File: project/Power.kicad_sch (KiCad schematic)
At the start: 20 parts, among them IC101 nPM1300-QEXX, X101 BATTERY

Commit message: Change layer for PCB tables to User1
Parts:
- C101, C110: Order Number 581-0603YC105JAT2A -> (none); Order. No. (none) -> 581-0603YC105JAT2A
- C102: Order Number 581-06035C104KAT2A -> (none); Order. No. (none) -> 581-06035C104KAT2A
- C103: Order Number 581-06036D225KAT2A -> (none); Order. No. (none) -> 581-06036D225KAT2A
- C104, C105, C106, C107, C108, C109: Order Number 346-CM105X5R106M25AT -> (none); Order. No. (none) -> 346-CM105X5R106M25AT
- IC101: Order Number 949-NPM1300-QEAA-R7 -> (none); Order. No. (none) -> 949-NPM1300-QEAA-R7
- L101, L102: Order Number 187-CIGT201610EH2R2M -> (none); Order. No. (none) -> 187-CIGT201610EH2R2MNE
- R101: Order Number 603-RC0603FR-0747KL -> (none); Order. No. (none) -> 603-RC0603FR-0747KL
- R102: Order Number 603-RC0603FR-07150KL -> (none); Order. No. (none) -> 603-RC0603FR-07150KL
- R103: Order Number 652-CR0603-J/-000ELF -> (none); Order. No. (none) -> 652-CR0603-J/-000ELF
- X101: Order Number 538-78171-0002 -> (none); Order. No. (none) -> 538-78171-0002
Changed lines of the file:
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@@
 			)
 		)
-		(property "Datasheet" "~"
+		(property "Datasheet" "https://www.mouser.de/datasheet/2/40/KGM_X7R-3223212.pdf"
 			(at 218.44 91.44 0)
 			(effects
@@
 			)
 		)
-		(property "Order Number" "581-0603YC105JAT2A"
+		(property "CONFIG" ""
 			(at 218.44 91.44 0)
 			(effects
@@
 			)
 		)
-		(property "CONFIG" ""
+		(property "Order. No." "581-0603YC105JAT2A"
 			(at 218.44 91.44 0)
 			(effects
@@
 			)
 		)
-		(property "Datasheet" "~"
+		(property "Datasheet" "https://www.mouser.de/datasheet/2/585/sems_s_a0006918008_1-2288745.pdf"
 			(at 173.99 106.68 0)
 			(effects
@@
 			)
 		)
-		(property "Order Number" "187-CIGT201610EH2R2M"
+		(property "CONFIG" ""
 			(at 173.99 106.68 0)
 			(effects
@@
 			)
 		)
-		(property "CONFIG" ""
+		(property "Order. No." "187-CIGT201610EH2R2MNE"
 			(at 173.99 106.68 0)
 			(effects
@@
 			)
 		)
-		(property "Datasheet" "~"
+		(property "Datasheet" "https://www.mouser.de/datasheet/2/40/KGM_X7R-3223212.pdf"
 			(at 113.03 44.45 0)
 			(effects
@@
 			)
 		)
-		(property "Order Number" "581-0603YC105JAT2A"
+		(property "CONFIG" ""
 			(at 113.03 44.45 0)
 			(effects
@@
 			)
 		)
-		(property "CONFIG" ""
+		(property "Order. No." "581-0603YC105JAT2A"
 			(at 113.03 44.45 0)
 			(effects
@@
 			)
 		)
-		(property "Datasheet" "~"
+		(property "Datasheet" "https://www.mouser.de/datasheet/2/40/CM_Series_e-2835982.pdf"
 			(at 184.15 109.22 0)
 			(effects
@@
 			)
 		)
-		(property "Order Number" "346-CM105X5R106M25AT"
+		(property "CONFIG" ""
 			(at 184.15 109.22 0)
 			(effects
@@
 			)
 		)
-		(property "CONFIG" ""
+		(property "Order. No." "346-CM105X5R106M25AT"
 			(at 184.15 109.22 0)
 			(effects
@@
 			)
 		)
-		(property "Order Number" "603-RC0603FR-07150KL"
+		(property "CONFIG" ""
 			(at 82.55 134.62 0)
 			(effects
@@
 			)
 		)
-		(property "CONFIG" ""
+		(property "Order. No." "603-RC0603FR-07150KL"
 			(at 82.55 134.62 0)
 			(effects
@@
 			)
 		)
-		(property "Order Number" ""
-			(at 200.66 125.73 0)
-			(effects
-				(font
-					(size 1.27 1.27)
-				)
-				(hide yes)
-			)
-		)
 		(property "CONFIG" ""
 			(at 200.66 125.73 0)
@@
 			)
 		)
-		(property "Datasheet" "~"
+		(property "Datasheet" "https://www.mouser.de/datasheet/2/40/CM_Series_e-2835982.pdf"
 			(at 193.04 91.44 0)
 			(effects
@@
 			)
 		)
-		(property "Order Number" "346-CM105X5R106M25AT"
+		(property "CONFIG" ""
 			(at 193.04 91.44 0)
 			(effects
@@
 			)
 		)
-		(property "CONFIG" ""
+		(property "Order. No." "346-CM105X5R106M25AT"
 			(at 193.04 91.44 0)
 			(effects
@@
 			)
 		)
-		(property "Order Number" "603-RC0603FR-0747KL"
+		(property "CONFIG" ""
 			(at 80.01 134.62 0)
 			(effects
@@
 			)
 		)
-		(property "CONFIG" ""
+		(property "Order. No." "603-RC0603FR-0747KL"
 			(at 80.01 134.62 0)
 			(effects
@@
 			)
 		)
-		(property "Order Number" "949-NPM1300-QEAA-R7"
+		(property "CONFIG" ""
 			(at 132.08 107.95 0)
 			(effects
@@
 			)
 		)
-		(property "CONFIG" ""
+		(property "Order. No." "949-NPM1300-QEAA-R7"
 			(at 132.08 107.95 0)
 			(effects
@@
 			)
 		)
-		(property "Datasheet" "~"
+		(property "Datasheet" "https://www.mouser.de/datasheet/2/40/CM_Series_e-2835982.pdf"
 			(at 191.77 63.5 0)
 			(effects
@@
 			)
 		)
-		(property "Order Number" "346-CM105X5R106M25AT"
+		(property "CONFIG" ""
 			(at 191.77 63.5 0)
 			(effects
@@
 			)
 		)
-		(property "CONFIG" ""
+		(property "Order. No." "346-CM105X5R106M25AT"
 			(at 191.77 63.5 0)
 			(effects
@@
 			)
 		)
-		(property "Datasheet" "~"
+		(property "Datasheet" "https://www.mouser.de/datasheet/2/585/sems_s_a0006918008_1-2288745.pdf"
 			(at 182.88 88.9 0)
 			(effects
@@
 			)
 		)
-		(property "Order Number" "187-CIGT201610EH2R2M"
+		(property "CONFIG" ""
 			(at 182.88 88.9 0)
 			(effects
@@
 			)
 		)
-		(property "CONFIG" ""
+		(property "Order. No." "187-CIGT201610EH2R2MNE"
 			(at 182.88 88.9 0)
 			(effects
@@
 			)
 		)
-		(property "Order Number" "538-78171-0002"
+		(property "CONFIG" ""
 			(at 158.75 40.64 0)
 			(effects
@@
 			)
 		)
-		(property "CONFIG" ""
+		(property "Order. No." "538-78171-0002"
 			(at 158.75 40.64 0)
 			(effects
@@
 			)
 		)
-		(property "Datasheet" "~"
+		(property "Datasheet" "https://www.mouser.de/datasheet/2/54/cr-1858361.pdf"
 			(at 135.89 63.5 0)
 			(effects
@@
 			)
 		)
-		(property "Order Number" "652-CR0603-J/-000ELF"
+		(property "CONFIG" ""
 			(at 135.89 63.5 0)
 			(effects
@@
 			)
 		)
-		(property "CONFIG" ""
+		(property "Order. No." "652-CR0603-J/-000ELF"
 			(at 135.89 63.5 0)
 			(effects
@@
 			)
 		)
-		(property "Datasheet" "~"
+		(property "Datasheet" "https://www.mouser.de/datasheet/2/40/CM_Series_e-2835982.pdf"
 			(at 181.61 63.5 0)
 			(effects
@@
 			)
 		)
-		(property "Order Number" "346-CM105X5R106M25AT"
+		(property "CONFIG" ""
 			(at 181.61 63.5 0)
 			(effects
@@
 			)
 		)
-		(property "CONFIG" ""
+		(property "Order. No." "346-CM105X5R106M25AT"
 			(at 181.61 63.5 0)
 			(effects
@@
 			)
 		)
-		(property "Datasheet" "~"
+		(property "Datasheet" "https://www.mouser.de/datasheet/2/40/cx5r_KGM-3223198.pdf"
 			(at 140.97 44.45 0)
 			(effects
@@
 			)
 		)
-		(property "Order Number" "581-06036D225KAT2A"
+		(property "CONFIG" ""
 			(at 140.97 44.45 0)
 			(effects
@@
 			)
 		)
-		(property "CONFIG" ""
+		(property "Order. No." "581-06036D225KAT2A"
 			(at 140.97 44.45 0)
 			(effects
@@
 			)
 		)
-		(property "Datasheet" "~"
+		(property "Datasheet" "https://www.mouser.de/datasheet/2/40/CM_Series_e-2835982.pdf"
 			(at 200.66 132.08 0)
 			(effects
@@
 			)
 		)
-		(property "Order Number" "346-CM105X5R106M25AT"
+		(property "CONFIG" ""
 			(at 200.66 132.08 0)
 			(effects
@@
 			)
 		)
-		(property "CONFIG" ""
+		(property "Order. No." "346-CM105X5R106M25AT"
 			(at 200.66 132.08 0)
 			(effects
@@
 			)
 		)
-		(property "Order Number" ""
-			(at 200.66 104.14 0)
-			(effects
-				(font
-					(size 1.27 1.27)
-				)
-				(hide yes)
-			)
-		)
 		(property "CONFIG" ""
 			(at 200.66 104.14 0)
@@
 			)
 		)
-		(property "Datasheet" "~"
+		(property "Datasheet" "https://www.mouser.de/datasheet/2/40/KGM_X7R-3223212.pdf"
 			(at 128.27 44.45 0)
 			(effects
@@
 			)
 		)
-		(property "Order Number" "581-06035C104KAT2A"
+		(property "CONFIG" ""
 			(at 128.27 44.45 0)
 			(effects
@@
 			)
 		)
-		(property "CONFIG" ""
+		(property "Order. No." "581-06035C104KAT2A"
 			(at 128.27 44.45 0)
 			(effects
@@
 			)
 		)
-		(property "Datasheet" "~"
+		(property "Datasheet" "https://www.mouser.de/datasheet/2/40/CM_Series_e-2835982.pdf"
 			(at 201.93 63.5 0)
 			(effects
@@
 			)
 		)
-		(property "Order Number" "346-CM105X5R106M25AT"
+		(property "CONFIG" ""
 			(at 201.93 63.5 0)
 			(effects
@@
 			)
 		)
-		(property "CONFIG" ""
+		(property "Order. No." "346-CM105X5R106M25AT"
 			(at 201.93 63.5 0)
 			(effects
@@
 			(at 200.66 86.36 0)
 			(effects
-				(font
-					(size 1.27 1.27)
-				)
-				(hide yes)
-			)
-		)
-		(property "Order Number" ""
-			(at 200.66 86.36 0)
-			(effects

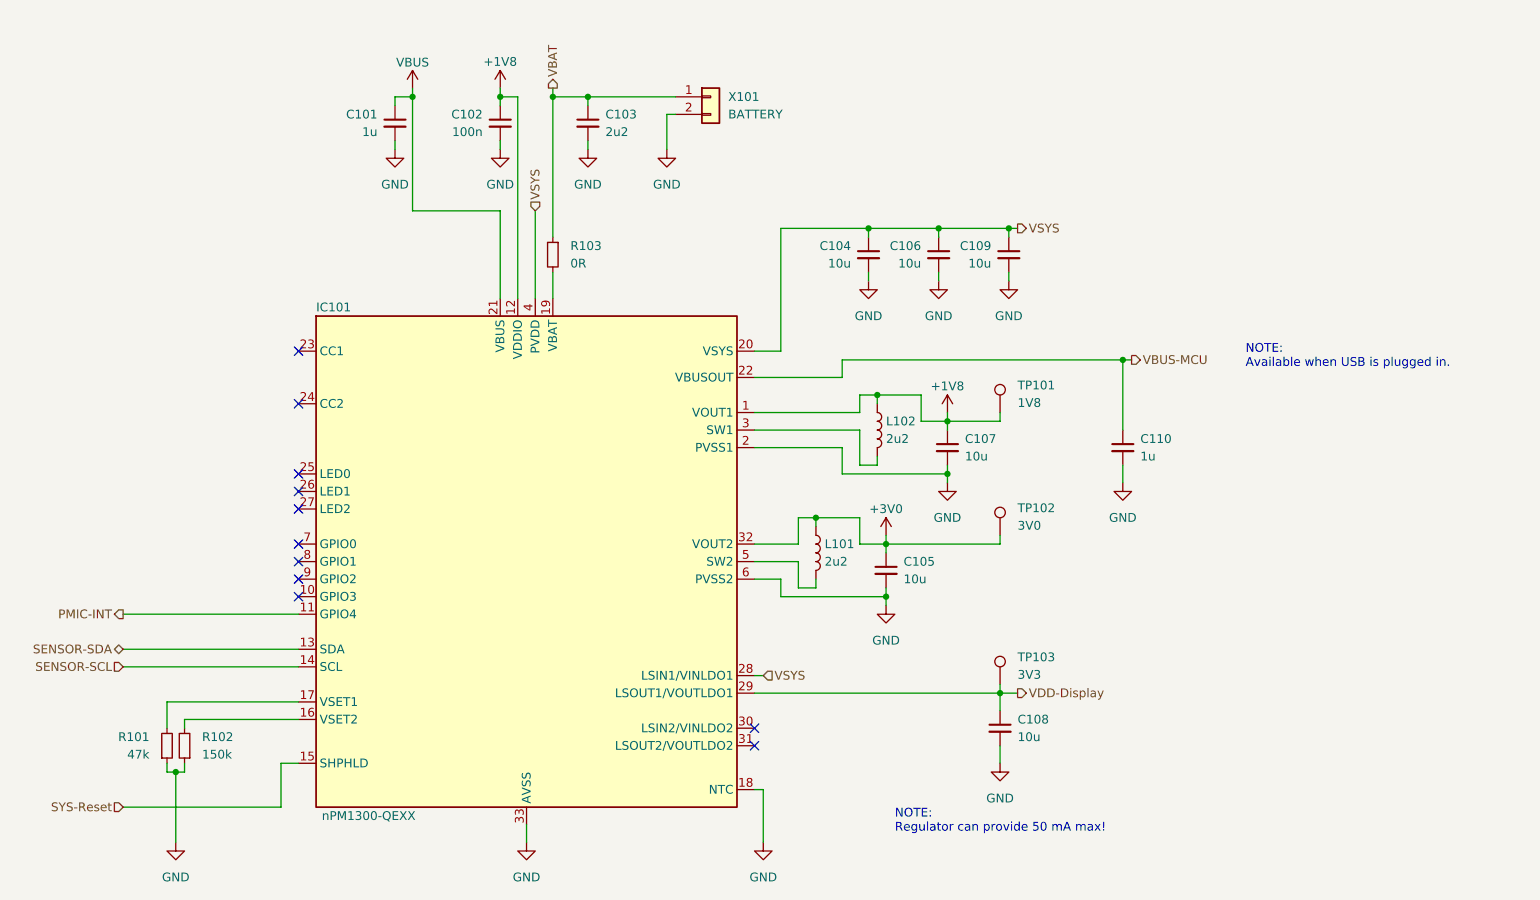
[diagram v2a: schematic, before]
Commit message: Rename signals and update symbols and footprints
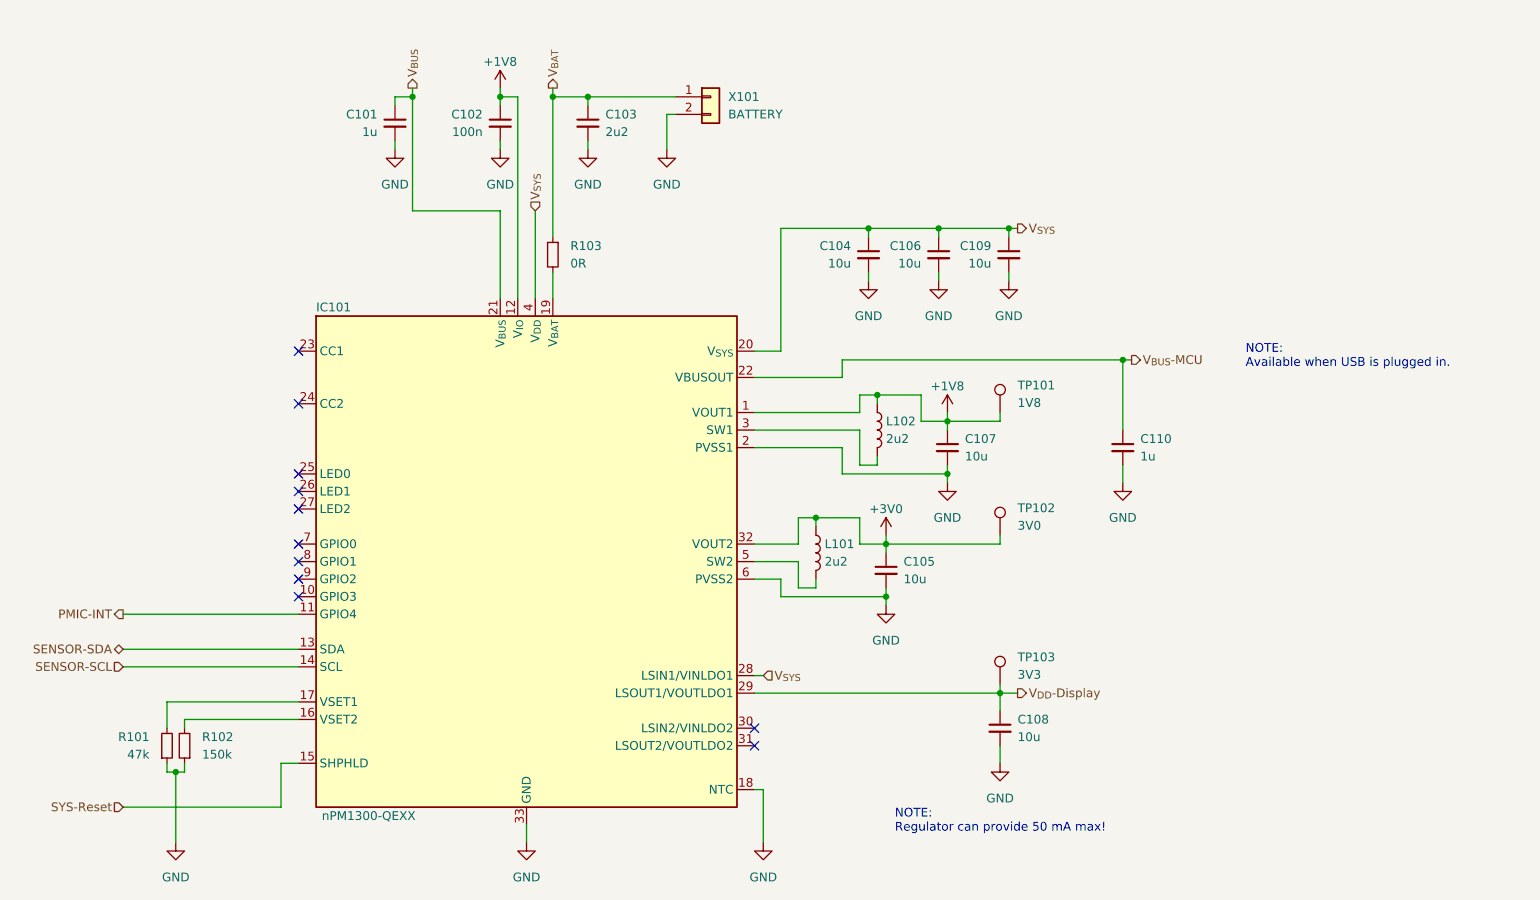
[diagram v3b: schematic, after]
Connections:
- net VBAT renamed V_{BAT}
- net VBUS renamed V_{BUS}
- net VBUS-MCU renamed V_{BUS}-MCU
- net VDD-Display renamed V_{DD}-Display
- net VSYS renamed V_{SYS}
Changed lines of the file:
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@@
 		)
 	)
-	(hierarchical_label "VSYS"
+	(hierarchical_label "V_{SYS}"
 		(shape output)
 		(at 203.2 59.69 0)
@@
 		)
 	)
-	(hierarchical_label "VBAT"
+	(hierarchical_label "V_{BAT}"
 		(shape output)
 		(at 135.89 39.37 90)
@@
 		)
 	)
-	(hierarchical_label "VBUS-MCU"
+	(hierarchical_label "V_{BUS}-MCU"
 		(shape output)
 		(at 219.71 78.74 0)
@@
 		)
 	)
-	(hierarchical_label "VSYS"
+	(hierarchical_label "V_{SYS}"
 		(shape input)
 		(at 166.37 124.46 0)
@@
 		)
 	)
-	(hierarchical_label "VDD-Display"
+	(hierarchical_label "V_{BUS}"
+		(shape output)
+		(at 115.57 39.37 90)
+		(fields_autoplaced yes)
+		(effects
+			(font
+				(size 1.27 1.27)
+			)
+			(justify left)
+		)
+	)
+	(hierarchical_label "V_{DD}-Display"
 		(shape output)
 		(at 203.2 127 0)
@@
 		)
 	)
-	(hierarchical_label "VSYS"
+	(hierarchical_label "V_{SYS}"
 		(shape input)
 		(at 133.35 57.15 90)
@@
 			)
 		)
-		(property "Description" ""
+		(property "Description" "Power symbol creates a global label with name \"GND\" , ground"
 			(at 184.15 114.3 0)
 			(effects
@@
 			)
 		)
-		(property "Description" ""
+		(property "Description" "Power symbol creates a global label with name \"+1V8\""
+			(at 128.27 39.37 0)
+			(effects
+				(font
+					(size 1.27 1.27)
+				)
+				(hide yes)
+			)
+		)
+		(property "Mfr." ""
+			(at 128.27 39.37 0)
+			(effects
+				(font
+					(size 1.27 1.27)
+				)
+				(hide yes)
+			)
+		)
+		(property "Mfr. No." ""
+			(at 128.27 39.37 0)
+			(effects
+				(font
+					(size 1.27 1.27)
+				)
+				(hide yes)
+			)
+		)
+		(property "Distributor" ""
+			(at 128.27 39.37 0)
+			(effects
+				(font
+					(size 1.27 1.27)
+				)
+				(hide yes)
+			)
+		)
+		(property "Order No." ""
+			(at 128.27 39.37 0)
+			(effects
+				(font
+					(size 1.27 1.27)
+				)
+				(hide yes)
+			)
+		)
+		(property "CONFIG" ""
 			(at 128.27 39.37 0)
 			(effects
@@
 			)
 		)
-		(property "Description" ""
+		(property "Description" "Power symbol creates a global label with name \"GND\" , ground"
 			(at 191.77 67.31 0)
 			(effects
@@
 			)
 		)
-		(property "Datasheet" "https://docs.nordicsemi.com/category/npm1300-category"
+		(property "Datasheet" "https://infocenter.nordicsemi.com/index.jsp?topic=%2Fstruct_pmic%2Fstruct%2Fnpm1300.html"
 			(at 132.08 110.49 0)
 			(effects
@@
 			)
 		)
+		(property "Order No." ""
+			(at 132.08 107.95 0)
+			(effects
+				(font
+					(size 1.27 1.27)
+				)
+				(hide yes)
+			)
+		)
 		(pin "1"
 		)
@@
 			)
 		)
-		(property "Description" ""
+		(property "Description" "Power symbol creates a global label with name \"+3V0\""
+			(at 184.15 104.14 0)
+			(effects
+				(font
+					(size 1.27 1.27)
+				)
+				(hide yes)
+			)
+		)
+		(property "Mfr." ""
+			(at 184.15 104.14 0)
+			(effects
+				(font
+					(size 1.27 1.27)
+				)
+				(hide yes)
+			)
+		)
+		(property "Mfr. No." ""
+			(at 184.15 104.14 0)
+			(effects
+				(font
+					(size 1.27 1.27)
+				)
+				(hide yes)
+			)
+		)
+		(property "Distributor" ""
+			(at 184.15 104.14 0)
+			(effects
+				(font
+					(size 1.27 1.27)
+				)
+				(hide yes)
+			)
+		)
+		(property "Order No." ""
+			(at 184.15 104.14 0)
+			(effects
+				(font
+					(size 1.27 1.27)
+				)
+				(hide yes)
+			)
+		)
+		(property "CONFIG" ""
 			(at 184.15 104.14 0)
 			(effects
@@
 			)
 		)
-		(property "Description" ""
+		(property "Description" "Power symbol creates a global label with name \"GND\" , ground"
 			(at 152.4 48.26 0)
 			(effects
@@
 			)
 		)
-		(property "Description" ""
+		(property "Description" "Power symbol creates a global label with name \"GND\" , ground"
 			(at 201.93 67.31 0)
 			(effects
@@
 			)
 		)
-		(property "Description" ""
+		(property "Description" "Power symbol creates a global label with name \"GND\" , ground"
 			(at 132.08 148.59 0)
 			(effects
@@
 			)
 		)
-		(property "Description" ""
+		(property "Description" "Power symbol creates a global label with name \"GND\" , ground"
 			(at 113.03 48.26 0)
 			(effects
@@
 			)
 		)
-		(property "Description" ""
+		(property "Description" "Power symbol creates a global label with name \"GND\" , ground"
 			(at 181.61 67.31 0)
 			(effects
@@
 			)
 		)
+		(property "Order No." ""
+			(at 181.61 67.31 0)
+			(effects
+				(font
+					(size 1.27 1.27)
+				)
+				(hide yes)
+			)
+		)
+		(property "CONFIG" ""
+			(at 181.61 67.31 0)
+			(effects
+				(font
+					(size 1.27 1.27)
+				)
+				(hide yes)
+			)
+		)
 		(pin "1"
 		)
@@
 			)
 		)
-		(property "Description" ""
+		(property "Description" "Power symbol creates a global label with name \"GND\" , ground"
 			(at 200.66 137.16 0)
 			(effects
@@
 			)
 		)
-		(property "Description" ""
+		(property "Description" "Power symbol creates a global label with name \"+1V8\""
 			(at 193.04 86.36 0)
 			(effects
@@
 			)
 		)
-		(property "Description" ""
+		(property "Description" "Power symbol creates a global label with name \"GND\" , ground"
 			(at 218.44 96.52 0)
 			(effects
@@
 	)
 	(symbol
-		(lib_id "power:VBUS")
-		(at 115.57 39.37 0)
-		(mirror y)
-		(unit 1)
-		(exclude_from_sim no)
-		(in_bom yes)
-		(on_board yes)
-		(dnp no)
-		(property "Reference" "#PWR0103"
-			(at 115.57 43.18 0)
-			(effects
-				(font
-					(size 1.27 1.27)
-				)
-				(hide yes)
-			)
-		)
-		(property "Value" "VBUS"
-			(at 115.57 35.6616 0)
-			(effects
-				(font
-					(size 1.27 1.27)
-				)
-			)
-		)
-		(property "Footprint" ""
-			(at 115.57 39.37 0)
-			(effects
-				(font
-					(size 1.27 1.27)
-				)
-				(hide yes)
-			)
-		)
-		(property "Datasheet" ""
-			(at 115.57 39.37 0)
-			(effects
-				(font
-					(size 1.27 1.27)
-				)
-				(hide yes)
-			)
-		)
-		(property "Description" ""
-			(at 115.57 39.37 0)
-			(effects
-				(font
-					(size 1.27 1.27)
-				)
-				(hide yes)
-			)
-		)
-		(property "Mfr." ""
-			(at 115.57 39.37 0)
-			(effects
-				(font
-					(size 1.27 1.27)
-				)
-				(hide yes)
-			)
-		)
-		(property "Mfr. No." ""
-			(at 115.57 39.37 0)
-			(effects
-				(font
-					(size 1.27 1.27)
-				)
-				(hide yes)
-			)
-		)
-		(property "Distributor" ""
-			(at 115.57 39.37 0)
-			(effects
-				(font
-					(size 1.27 1.27)
-				)
-				(hide yes)
-			)
-		)
-		(property "Order Number" ""
-			(at 115.57 39.37 0)
-			(effects
-				(font
-					(size 1.27 1.27)
-				)
-				(hide yes)
-			)
-		)
-		(pin "1"
-		)
-		(instances
-			(project "ZSWatch"
-				(path "/d5742f03-3b1a-42e5-a384-018bd4b919aa/cee9a3a2-28cd-4e6c-b23d-337f115f39e8"
-					(reference "#PWR0103")
-					(unit 1)
-				)
-			)
-		)
-	)
-	(symbol
 		(lib_id "Device:C_Small")
 		(at 128.27 44.45 0)
@@
 			)
 		)
-		(property "Description" ""
+		(property "Description" "Power symbol creates a global label with name \"GND\" , ground"
 			(at 166.37 148.59 0)
 			(effects
@@
 			)
 		)
-		(property "Description" ""
+		(property "Description" "Power symbol creates a global label with name \"GND\" , ground"
 			(at 140.97 48.26 0)
 			(effects
@@
 			)
 		)
-		(property "Description" ""
+		(property "Description" "Power symbol creates a global label with name \"GND\" , ground"
 			(at 193.04 96.52 0)
 			(effects
@@
 			)
 		)
-		(property "Description" ""
+		(property "Description" "Power symbol creates a global label with name \"GND\" , ground"
 			(at 128.27 48.26 0)
 			(effects
@@
 			)
 		)
-		(property "Description" ""
+		(property "Description" "Power symbol creates a global label with name \"GND\" , ground"
 			(at 81.28 148.59 0)
 			(effects

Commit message: - Switch to a local KiCad library
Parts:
- IC101: footprint Package_DFN_QFN:QFN-32-1EP_5x5mm_P0.5mm_EP3.6x3.6mm_ThermalVias -> Package_DFN_QFN:QFN-32-1EP_5x5mm_P0.5mm_EP3.6x3.6mm
- L101, L102: footprint Inductor_SMD_Kampi:L_0806_2016 -> Inductor_SMD:L_0806_2016
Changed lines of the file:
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@@
 			)
 		)
-		(property "Footprint" "Inductor_SMD_Kampi:L_0806_2016"
+		(property "Footprint" "Inductor_SMD:L_0806_2016"
 			(at 173.99 106.68 0)
 			(effects
@@
 		)
 		(property "Order. No." "187-CIGT201610EH2R2MNE"
+			(at 173.99 106.68 0)
+			(effects
+				(font
+					(size 1.27 1.27)
+				)
+				(hide yes)
+			)
+		)
+		(property "Order No." ""
 			(at 173.99 106.68 0)
 			(effects
@@
 			)
 		)
-		(property "Footprint" "Package_DFN_QFN:QFN-32-1EP_5x5mm_P0.5mm_EP3.6x3.6mm_ThermalVias"
+		(property "Footprint" "Package_DFN_QFN:QFN-32-1EP_5x5mm_P0.5mm_EP3.6x3.6mm"
 			(at 132.08 107.95 0)
 			(effects
@@
 			)
 		)
-		(property "Footprint" "Inductor_SMD_Kampi:L_0806_2016"
+		(property "Footprint" "Inductor_SMD:L_0806_2016"
 			(at 182.88 88.9 0)
 			(effects
@@
 			(at 182.88 88.9 0)
 			(effects
+				(font
+					(size 1.27 1.27)
+				)
+				(hide yes)
+			)
+		)
+		(property "Order No." ""
+			(at 182.88 88.9 0)
+			(effects
